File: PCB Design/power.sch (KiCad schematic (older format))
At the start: 15 parts, among them P1 CONN_01X03, P2 CONN_01X02, U1 3.3VREG

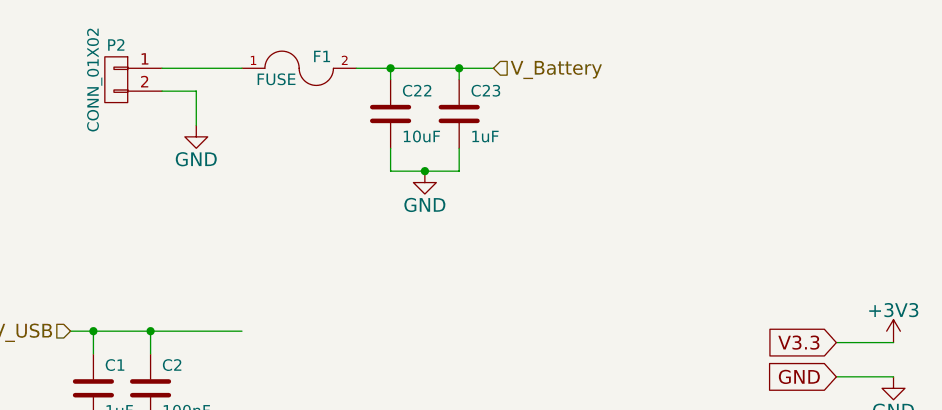
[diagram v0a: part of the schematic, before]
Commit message: Changed power input to diode and fuse, fixed pinout
The power input is now protected by a diode and fuse in series.
The pinout of the PIC is fixed, pin 17 is now RB6 rather than RA6

Signed-off-by: Kolijn Wolfaardt <kolijn.wolfaardt@gmail.com>
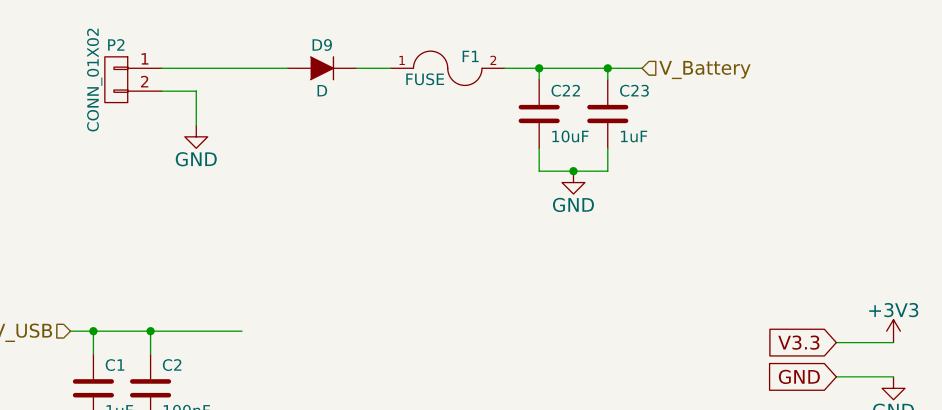
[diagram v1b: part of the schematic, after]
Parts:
- added D9: D, symbol D
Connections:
- net at P2.1 (P1): now also D9.1 (A); no longer F1.1
- new net: D9.2 (K), F1.1
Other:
- moved on the sheet: C22, C23, F1
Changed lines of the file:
@@
 Wire Wire Line
 	3550 1150 3550 1300
-Text HLabel 4850 1050 2    60   Input ~ 0
+Text HLabel 5500 1050 2    60   Input ~ 0
 V_Battery
 $Comp
 L FUSE F1
 U 1 1 551265E8
-P 4000 1050
-F 0 "F1" H 4100 1100 50  0000 C CNN
-F 1 "FUSE" H 3900 1000 50  0000 C CNN
-F 2 "" H 4000 1050 60  0000 C CNN
-F 3 "" H 4000 1050 60  0000 C CNN
-	1    4000 1050
+P 4650 1050
+F 0 "F1" H 4750 1100 50  0000 C CNN
+F 1 "FUSE" H 4550 1000 50  0000 C CNN
+F 2 "" H 4650 1050 60  0000 C CNN
+F 3 "" H 4650 1050 60  0000 C CNN
+	1    4650 1050
 	1    0    0    -1
 $EndComp
 Wire Wire Line
-	3400 1050 3750 1050
+	3400 1050 3950 1050
 Wire Wire Line
 	5000 3900 5000 3950
@@
 V_USB
 Wire Wire Line
-	4250 1050 4850 1050
+	4900 1050 5500 1050
 $Comp
 L C C22
 U 1 1 5513C923
-P 4400 1250
-F 0 "C22" H 4450 1350 50  0000 L CNN
-F 1 "10uF" H 4450 1150 50  0000 L CNN
-F 2 "" H 4438 1100 30  0000 C CNN
-F 3 "" H 4400 1250 60  0000 C CNN
-	1    4400 1250
+P 5050 1250
+F 0 "C22" H 5100 1350 50  0000 L CNN
+F 1 "10uF" H 5100 1150 50  0000 L CNN
+F 2 "" H 5088 1100 30  0000 C CNN
+F 3 "" H 5050 1250 60  0000 C CNN
+	1    5050 1250
 	1    0    0    -1
 $EndComp
@@
 L C C23
 U 1 1 5513C9DF
-P 4700 1250
-F 0 "C23" H 4750 1350 50  0000 L CNN
-F 1 "1uF" H 4750 1150 50  0000 L CNN
-F 2 "" H 4738 1100 30  0000 C CNN
-F 3 "" H 4700 1250 60  0000 C CNN
-	1    4700 1250
+P 5350 1250
+F 0 "C23" H 5400 1350 50  0000 L CNN
+F 1 "1uF" H 5400 1150 50  0000 L CNN
+F 2 "" H 5388 1100 30  0000 C CNN
+F 3 "" H 5350 1250 60  0000 C CNN
+	1    5350 1250
 	1    0    0    -1
 $EndComp
 Wire Wire Line
-	4700 1100 4700 1050
-Connection ~ 4700 1050
+	5350 1100 5350 1050
+Connection ~ 5350 1050
 Wire Wire Line
-	4400 1100 4400 1050
-Connection ~ 4400 1050
+	5050 1100 5050 1050
+Connection ~ 5050 1050
 $Comp
 L GND #PWR07
 U 1 1 5513CAE7
-P 4550 1500
-F 0 "#PWR07" H 4550 1250 60  0001 C CNN
-F 1 "GND" H 4550 1350 60  0000 C CNN
-F 2 "" H 4550 1500 60  0000 C CNN
-F 3 "" H 4550 1500 60  0000 C CNN
-	1    4550 1500
+P 5200 1500
+F 0 "#PWR07" H 5200 1250 60  0001 C CNN
+F 1 "GND" H 5200 1350 60  0000 C CNN
+F 2 "" H 5200 1500 60  0000 C CNN
+F 3 "" H 5200 1500 60  0000 C CNN
+	1    5200 1500
 	1    0    0    -1
 $EndComp
 Wire Wire Line
-	4400 1500 4700 1500
+	5050 1500 5350 1500
 Wire Wire Line
-	4700 1500 4700 1400
+	5350 1500 5350 1400
 Wire Wire Line
-	4400 1500 4400 1400
-Connection ~ 4550 1500
+	5050 1500 5050 1400
+Connection ~ 5200 1500
+$Comp
+L D D9
+U 1 1 5513F6F1
+P 4100 1050
+F 0 "D9" H 4100 1150 50  0000 C CNN
+F 1 "D" H 4100 950 50  0000 C CNN
+F 2 "" H 4100 1050 60  0000 C CNN
+F 3 "" H 4100 1050 60  0000 C CNN
+	1    4100 1050
+	1    0    0    -1
+$EndComp
+Wire Wire Line
+	4400 1050 4250 1050
 $EndSCHEMATC

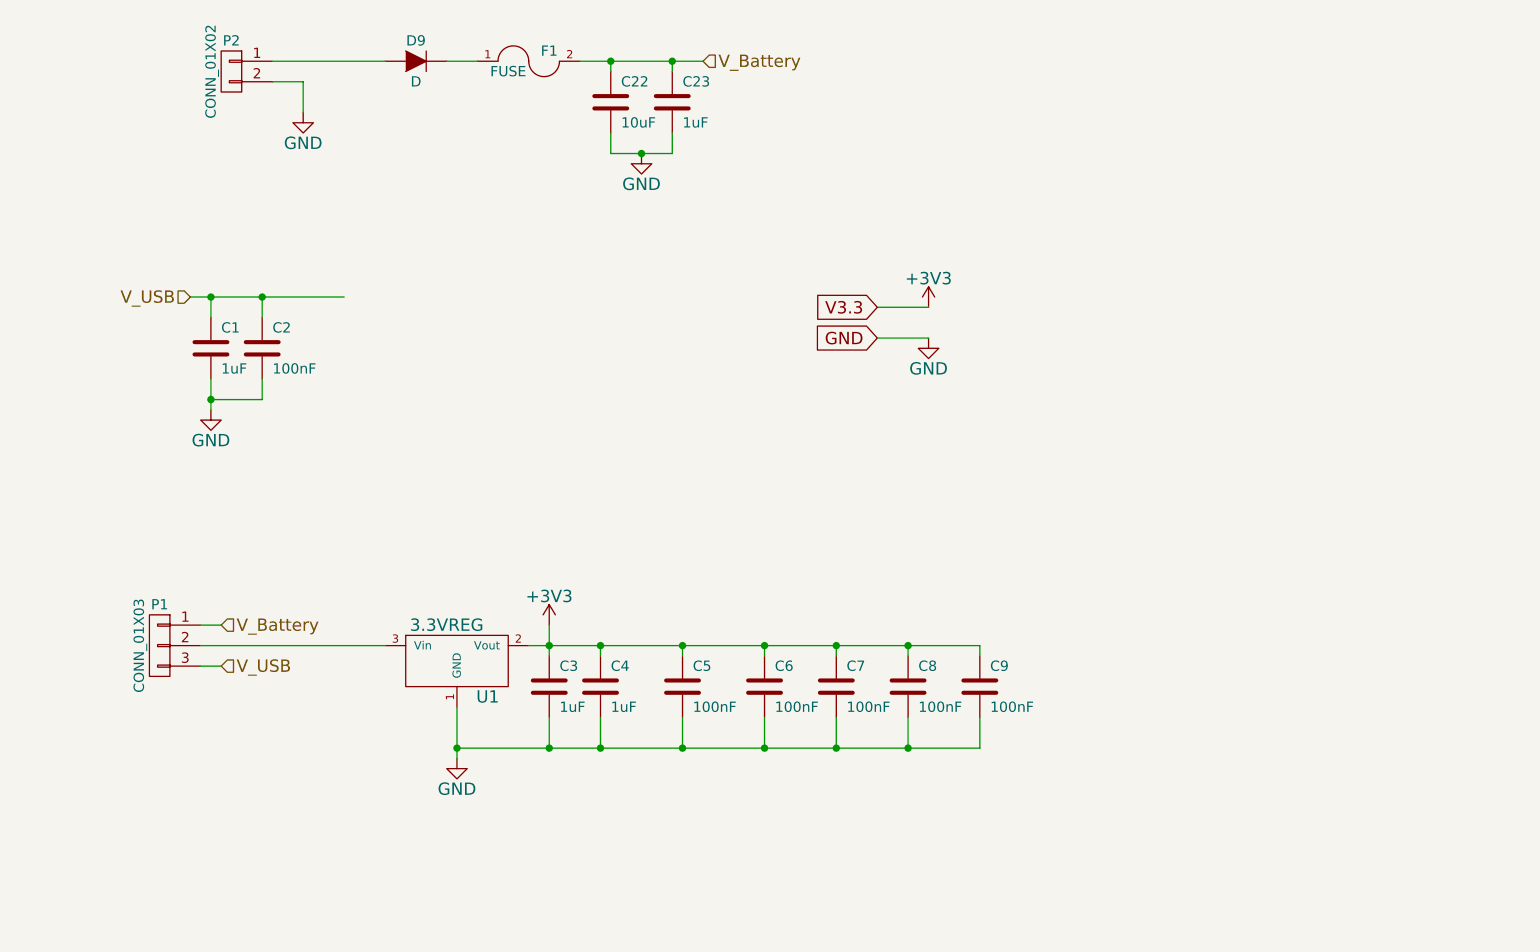
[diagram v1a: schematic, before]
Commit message: Added initial footprint associations, caps and resistors.
Kicad is giving weird errors for the libraries and BOM generator.
The libraries have to be downloaded manually from github, and
then added.

Signed-off-by: Kolijn Wolfaardt <kolijn.wolfaardt@gmail.com>
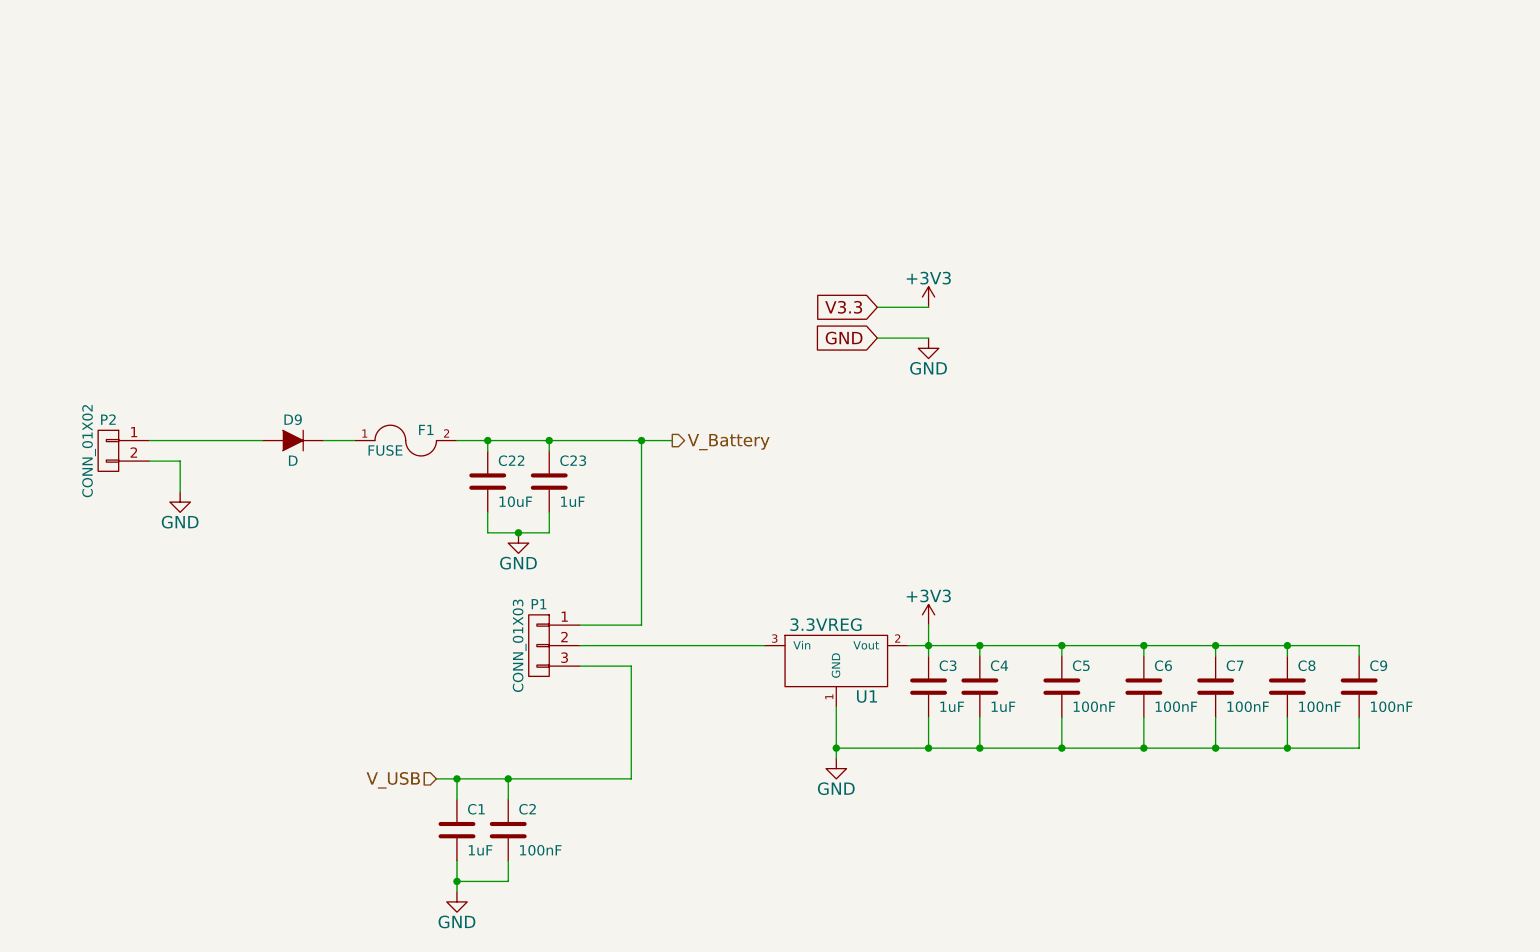
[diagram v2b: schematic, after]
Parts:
- C1, C2, C22, C23, C3, C4, C5, C6, C7, C8, C9: footprint (none) -> Capacitors_SMD:C_1206
- D9: footprint (none) -> Diode
- P1: footprint (none) -> Pin_Headers:Pin_Header_Straight_1x03
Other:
- moved on the sheet: C1, C2, C22, C23, C3, C4, C5, C6, C7, C8, C9, D9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

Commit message: Added diodes to motor driver
Signed-off-by: Kolijn_Laptop <kolijn.wolfaardt@gmail.com>
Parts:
- added D18: LED, symbol LED
- added R15: R, symbol R
- D9: footprint Diode -> (none)
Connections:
- net +3V3: now also D18.1 (A)
- net GND: now also R15.2
- new net: D18.2 (K), R15.1
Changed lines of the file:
@@
 $EndComp
 Wire Wire Line
-	6500 3900 8700 3900
+	6500 3900 9350 3900
 Wire Wire Line
 	6600 3800 6600 3950
@@
 F 0 "D9" H 3500 3000 50  0000 C CNN
 F 1 "D" H 3500 2800 50  0000 C CNN
-F 2 "Diode" H 3500 2900 60  0001 C CNN
+F 2 "" H 3500 2900 60  0001 C CNN
 F 3 "" H 3500 2900 60  0000 C CNN
 	1    3500 2900
@@
 V_Battery
 Connection ~ 5200 2900
+$Comp
+L LED D18
+U 1 1 551840ED
+P 9350 4150
+F 0 "D18" H 9350 4250 50  0000 C CNN
+F 1 "LED" H 9350 4050 50  0000 C CNN
+F 2 "" H 9350 4150 60  0001 C CNN
+F 3 "" H 9350 4150 60  0000 C CNN
+	1    9350 4150
+	0    1    1    0
+$EndComp
+$Comp
+L R R15
+U 1 1 55184149
+P 9350 4550
+F 0 "R15" V 9430 4550 50  0000 C CNN
+F 1 "R" V 9350 4550 50  0000 C CNN
+F 2 "" V 9280 4550 30  0001 C CNN
+F 3 "" H 9350 4550 30  0000 C CNN
+	1    9350 4550
+	1    0    0    -1
+$EndComp
+$Comp
+L GND #PWR08
+U 1 1 551841D4
+P 9350 4750
+F 0 "#PWR08" H 9350 4500 60  0001 C CNN
+F 1 "GND" H 9350 4600 60  0000 C CNN
+F 2 "" H 9350 4750 60  0000 C CNN
+F 3 "" H 9350 4750 60  0000 C CNN
+	1    9350 4750
+	1    0    0    -1
+$EndComp
+Wire Wire Line
+	9350 4700 9350 4750
+Wire Wire Line
+	9350 4400 9350 4350
+Wire Wire Line
+	9350 3900 9350 3950
+Connection ~ 8700 3900
 $EndSCHEMATC

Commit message: Added crystal footprint
Signed-off-by: Kolijn Wolfaardt <kolijn.wolfaardt@gmail.com>
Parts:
- R15: value R -> 220; footprint (none) -> Resistors_SMD:R_1206
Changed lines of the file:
@@
 $EndDescr
 $Comp
-L +3V3 #PWR01
+L +3V3 #PWR5
 U 1 1 551253EA
 P 6600 2250
-F 0 "#PWR01" H 6600 2100 60  0001 C CNN
+F 0 "#PWR5" H 6600 2100 60  0001 C CNN
 F 1 "+3V3" H 6600 2390 60  0000 C CNN
 F 2 "" H 6600 2250 60  0000 C CNN
@@
 $EndComp
 $Comp
-L GND #PWR02
+L GND #PWR6
 U 1 1 551253F0
 P 6600 2400
-F 0 "#PWR02" H 6600 2150 60  0001 C CNN
+F 0 "#PWR6" H 6600 2150 60  0001 C CNN
 F 1 "GND" H 6600 2250 60  0000 C CNN
 F 2 "" H 6600 2400 60  0000 C CNN
@@
 $EndComp
 $Comp
-L +3V3 #PWR03
+L +3V3 #PWR7
 U 1 1 551258E1
 P 6600 3800
-F 0 "#PWR03" H 6600 3650 60  0001 C CNN
+F 0 "#PWR7" H 6600 3650 60  0001 C CNN
 F 1 "+3V3" H 6600 3940 60  0000 C CNN
 F 2 "" H 6600 3800 60  0000 C CNN
@@
 	6600 3800 6600 3950
 $Comp
-L GND #PWR04
+L GND #PWR4
 U 1 1 55125915
 P 6150 4450
-F 0 "#PWR04" H 6150 4200 60  0001 C CNN
+F 0 "#PWR4" H 6150 4200 60  0001 C CNN
 F 1 "GND" H 6150 4300 60  0000 C CNN
 F 2 "" H 6150 4450 60  0000 C CNN
@@
 $EndComp
 $Comp
-L GND #PWR05
+L GND #PWR2
 U 1 1 55125A29
 P 4300 5100
-F 0 "#PWR05" H 4300 4850 60  0001 C CNN
+F 0 "#PWR2" H 4300 4850 60  0001 C CNN
 F 1 "GND" H 4300 4950 60  0000 C CNN
 F 2 "" H 4300 5100 60  0000 C CNN
@@
 $EndComp
 $Comp
-L GND #PWR06
+L GND #PWR1
 U 1 1 551264A9
 P 2950 3150
-F 0 "#PWR06" H 2950 2900 60  0001 C CNN
+F 0 "#PWR1" H 2950 2900 60  0001 C CNN
 F 1 "GND" H 2950 3000 60  0000 C CNN
 F 2 "" H 2950 3150 60  0000 C CNN
@@
 Connection ~ 4450 2900
 $Comp
-L GND #PWR07
+L GND #PWR3
 U 1 1 5513CAE7
 P 4600 3350
-F 0 "#PWR07" H 4600 3100 60  0001 C CNN
+F 0 "#PWR3" H 4600 3100 60  0001 C CNN
 F 1 "GND" H 4600 3200 60  0000 C CNN
 F 2 "" H 4600 3350 60  0000 C CNN
@@
 P 9350 4550
 F 0 "R15" V 9430 4550 50  0000 C CNN
-F 1 "R" V 9350 4550 50  0000 C CNN
-F 2 "" V 9280 4550 30  0001 C CNN
+F 1 "220" V 9350 4550 50  0000 C CNN
+F 2 "Resistors_SMD:R_1206" V 9280 4550 30  0001 C CNN
 F 3 "" H 9350 4550 30  0000 C CNN
 	1    9350 4550
@@
 $EndComp
 $Comp
-L GND #PWR08
+L GND #PWR8
 U 1 1 551841D4
 P 9350 4750
-F 0 "#PWR08" H 9350 4500 60  0001 C CNN
+F 0 "#PWR8" H 9350 4500 60  0001 C CNN
 F 1 "GND" H 9350 4600 60  0000 C CNN
 F 2 "" H 9350 4750 60  0000 C CNN
